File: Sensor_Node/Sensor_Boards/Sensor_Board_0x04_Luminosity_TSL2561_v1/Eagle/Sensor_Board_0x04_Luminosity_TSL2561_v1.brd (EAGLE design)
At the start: 55 x 35 mm, 15 parts, among them J1 M04_SMD_90, J2 M06_SMD_STRAIGHT, J4 ARDUINO_ISP, U2 ATMEGA328P_TQFP, Y1 8MHZ

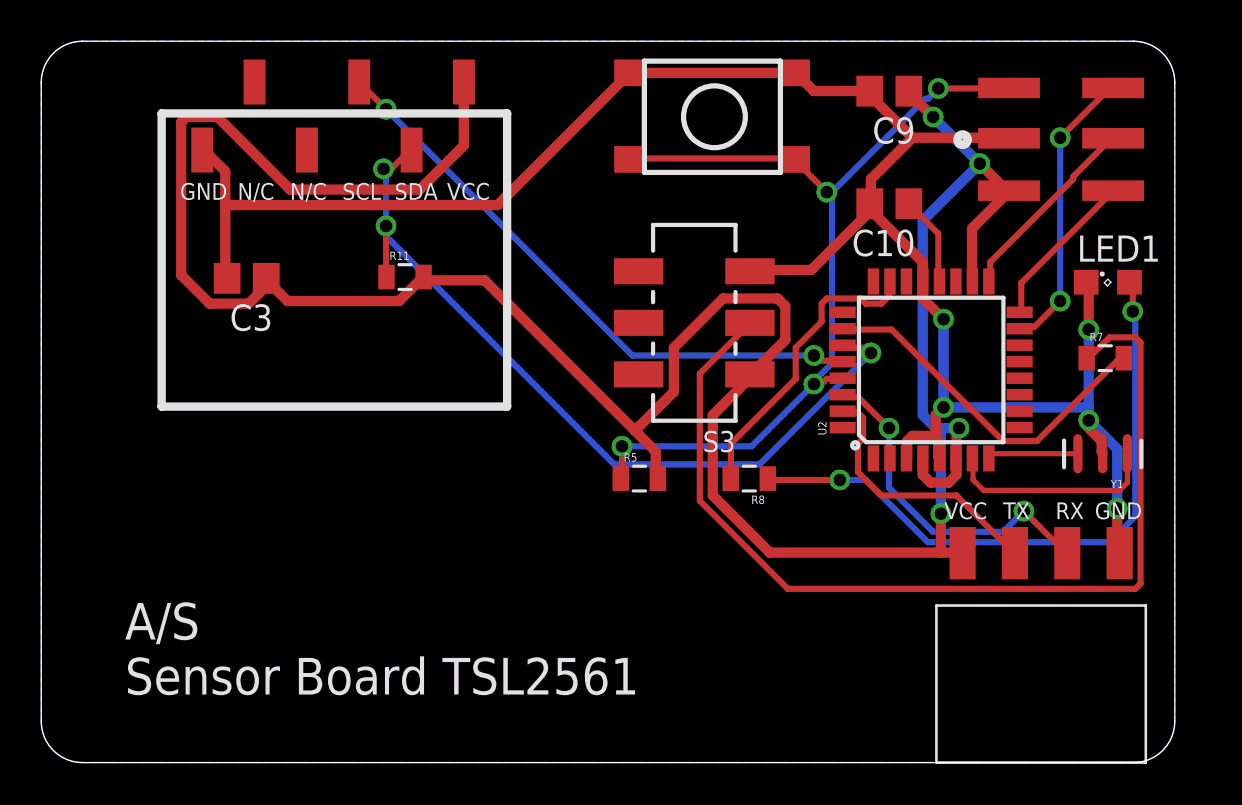
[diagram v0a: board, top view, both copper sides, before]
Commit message: Changes on SensModule TSL2561
- removed R11
- added pogohead programming connector
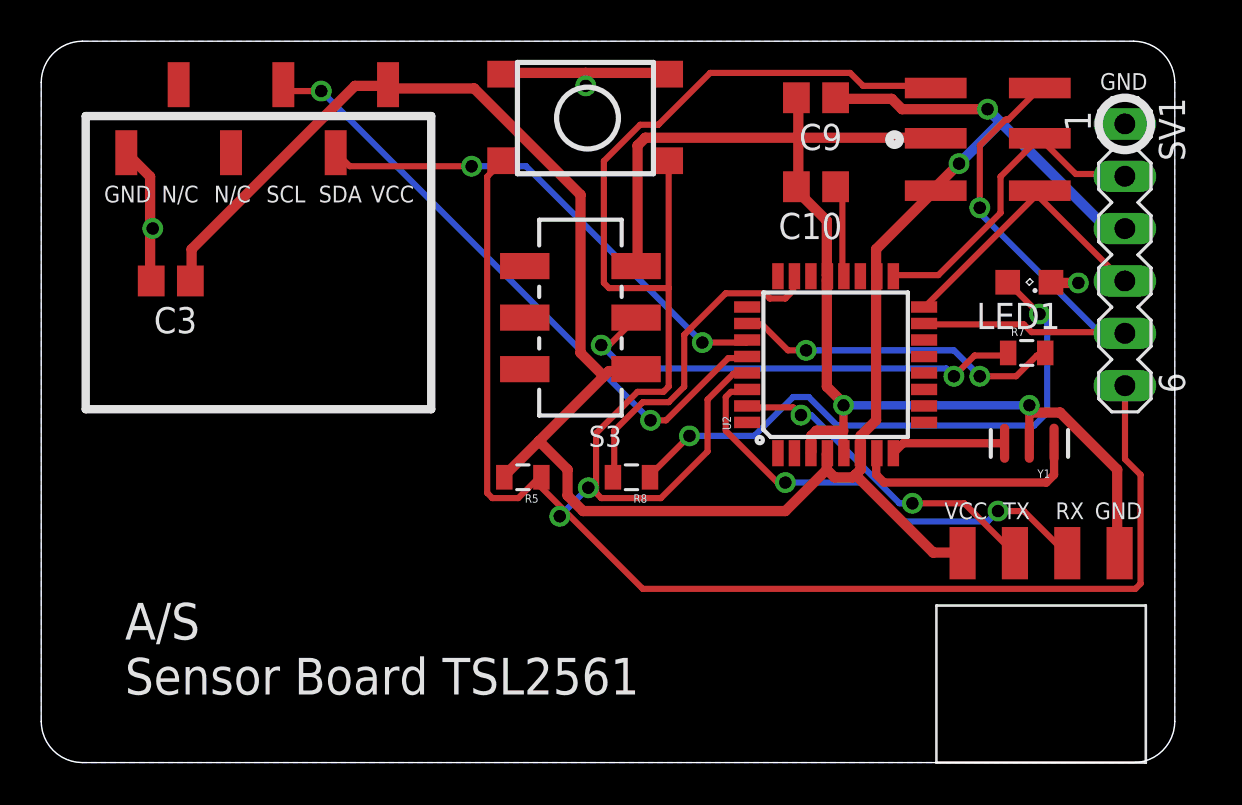
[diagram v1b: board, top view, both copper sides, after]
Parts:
- removed R11: 10k, SparkFun-Passives:0805
- added SV1: (no value), con-lstb:MA06-1
- moved S1 6.16 mm to (22.4, 33.4)
- moved R8 5.72 mm to (28.6, 13.8)
- moved R5 5.65 mm to (23.4, 13.8), turned to 180 degrees
- moved S3 5.53 mm to (26.2, 21.6)
- moved U2 4.64 mm to (38.5, 19.3)
- moved R7 3.82 mm to (47.8, 19.9)
- moved LED1 3.81 mm to (47.9, 23.3), turned to 180 degrees
- moved C3 3.69 mm to (6.29, 23.4)
- moved J2 3.69 mm to (4.13, 29.6)
- moved C10 3.65 mm to (37.6, 27.9)
- moved Y1 3.59 mm to (47.9, 15.5)
- moved C9 3.57 mm to (37.6, 32.3)
- moved J4 3.56 mm to (48.5, 27.7)
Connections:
- net GND: now also SV1.1
- net MISO: now also SV1.4
- net MOSI: now also SV1.5
- net RESET: now also SV1.6
- net SCK: now also SV1.2
- net SDA: no longer R11.1
- net VCC: now also SV1.3; no longer R11.2
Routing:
- net RESET: track 44.5 -> 121.2 mm, vias 4 -> 2
- net N$3: track 47.7 -> 23.1 mm, vias 0 -> 2
- net VCC: track 130.6 -> 106.7 mm, vias 4 -> 2
- net GND: track 99.5 -> 78.8 mm
- net SDA: track 39.4 -> 23.9 mm, vias 3 -> 2
- net MOSI: track 14.1 -> 26.7 mm, vias 2 -> 1
- net MISO: track 7.79 -> 14.2 mm
- net SCK: track 9.51 -> 15.8 mm
- net MCU_RXI: track 16.6 -> 22.3 mm
- net MCU_TXO: track 13.1 -> 15.9 mm, vias 0 -> 2
- net N$30: track 31.1 -> 28.9 mm
- net DBG_ENABLE: track 17.6 -> 16.0 mm, vias 0 -> 2
- net L1: track 14.7 -> 16.2 mm
- net SCL: track 29.1 -> 30.5 mm
- net N$2: track 10.3 -> 11.5 mm
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
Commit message: Changes on all boards
- added capacitor on reset-path
- changed order of pogopin programmer pins

Pulse-Board:
- Deleted input-jumper. Currently one interrupt-pin missing, so print is
not yet routed.
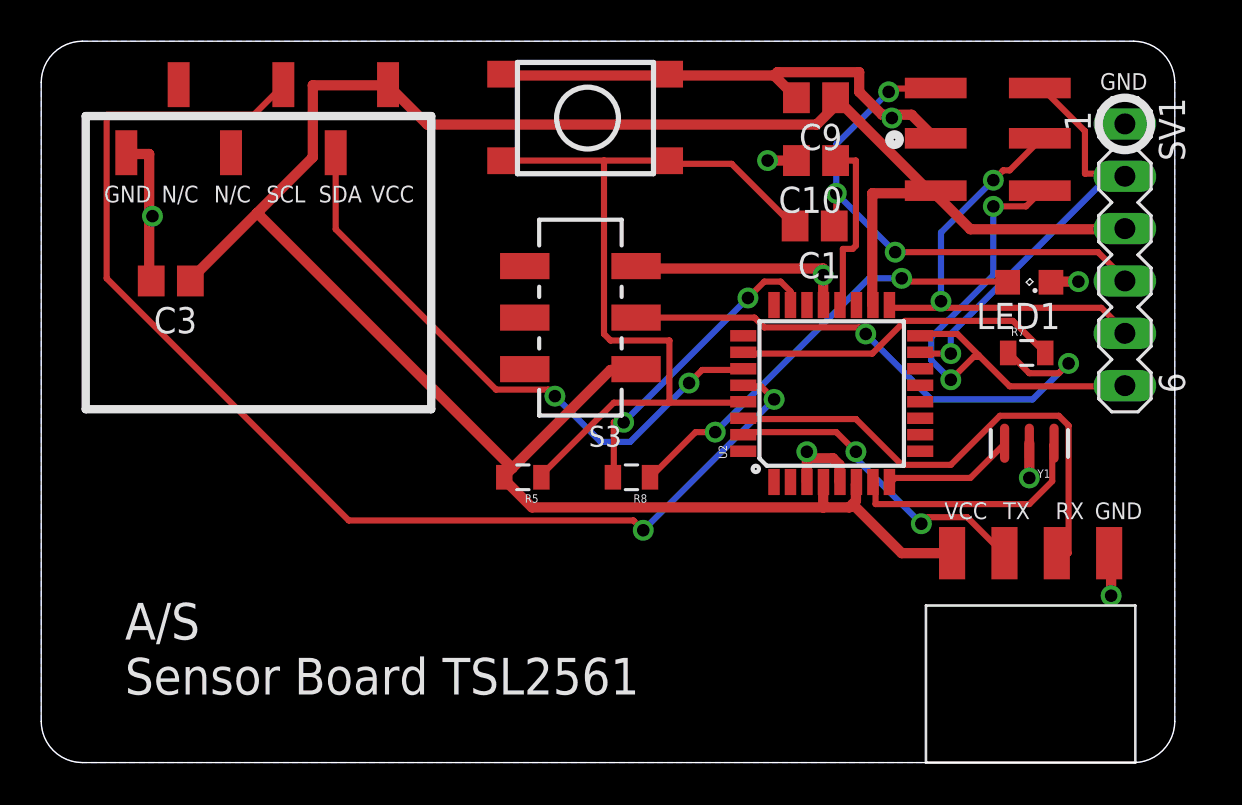
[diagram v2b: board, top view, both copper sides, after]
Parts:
- added C1: 100n, eagle-ltspice:C0805
- moved U2 1.41 mm to (38.4, 17.9)
- moved C10 1.27 mm to (37.6, 29.2)
- moved J1 0.51 mm to (44.2, 10.2)
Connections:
- new net N$4: C1.2, R5.1, S1.3, S1.4, U2.29
- net MISO: now also SV1.6; no longer SV1.4
- net MOSI: now also SV1.2; no longer SV1.5
- net RESET: now also C1.1, SV1.4; no longer R5.1, S1.3, S1.4, SV1.6, U2.29
- net SCK: now also SV1.5; no longer SV1.2
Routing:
- net RESET: track 121.2 -> 25.8 mm, vias 2 -> 3
- net N$4: track 0.00 -> 41.6 mm
- net SCL: track 30.5 -> 59.0 mm
- net GND: track 78.8 -> 53.7 mm, vias 5 -> 8
- net MISO: track 14.2 -> 25.6 mm, vias 0 -> 2
- net VCC: track 106.7 -> 116.2 mm, vias 2 -> 0
- net N$30: track 28.9 -> 21.4 mm
- net SCK: track 15.8 -> 22.4 mm, vias 0 -> 2
- net MOSI: track 26.7 -> 21.2 mm
- net SDA: track 23.9 -> 29.2 mm
- net N$15: track 4.55 -> 8.66 mm
- net N$3: track 23.1 -> 26.9 mm
- net MCU_RXI: track 22.3 -> 24.7 mm, vias 2 -> 0
- net L1: track 16.2 -> 14.9 mm, vias 0 -> 2
- net N$1: track 5.60 -> 6.37 mm
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
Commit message: Changed some SensorBoards
SHT31
- new routing

PULSE
- pogopin programmer now over FTDI
- interrupt to comboard now comes from atmega

TSL2561
- pogopin programmer now over FTDI

PROTOYPING
- changed title of schematic
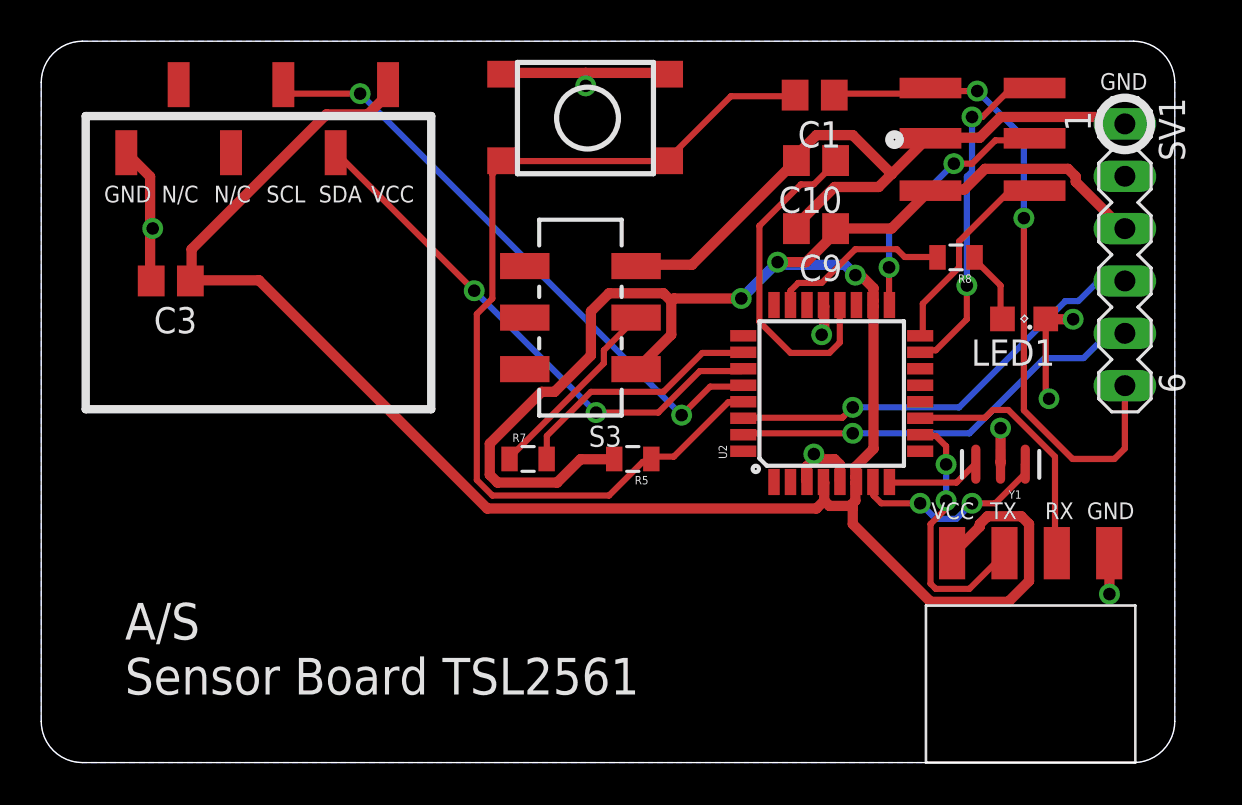
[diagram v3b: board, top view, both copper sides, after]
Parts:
- moved R7 24.7 mm to (23.6, 14.7)
- moved R8 19.0 mm to (44.4, 24.5)
- moved C9 6.35 mm to (37.6, 25.9)
- moved C1 6.35 mm to (37.5, 32.4)
- moved R5 5.41 mm to (28.7, 14.7)
- moved LED1 1.80 mm to (47.7, 21.5)
- moved Y1 1.73 mm to (46.5, 14.5)
- moved J4 0.25 mm to (48.2, 27.7)
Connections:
- new net FTDI_RXI: SV1.4, U2.30
- new net FTDI_TXO: SV1.5, U2.31
- net GND: now also SV1.2
- net MCU_RXI: now also U2.11; no longer U2.30
- net MCU_TXO: now also U2.10; no longer U2.31
- net MISO: no longer SV1.6
- net MOSI: no longer SV1.2
- net RESET: now also SV1.6; no longer SV1.4
- net SCK: no longer SV1.5
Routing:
- net SCL: track 59.0 -> 29.5 mm
- net VCC: track 116.2 -> 139.2 mm, vias 0 -> 3
- net FTDI_RXI: track 0.00 -> 21.3 mm, vias 0 -> 1
- net FTDI_TXO: track 0.00 -> 20.6 mm, vias 0 -> 1
- net N$30: track 21.4 -> 3.54 mm, vias 2 -> 0
- net N$3: track 26.9 -> 9.39 mm, vias 2 -> 0
- net MISO: track 25.6 -> 10.1 mm, vias 2 -> 0
- net MCU_RXI: track 24.7 -> 12.4 mm
- net GND: track 53.7 -> 64.1 mm
- net SCK: track 22.4 -> 12.6 mm
- net N$15: track 8.66 -> 16.4 mm
- net RESET: track 25.8 -> 32.8 mm, vias 3 -> 2
- net L1: track 14.9 -> 8.82 mm, vias 2 -> 0
- net N$4: track 41.6 -> 46.7 mm
- net MOSI: track 21.2 -> 16.5 mm, vias 1 -> 2
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
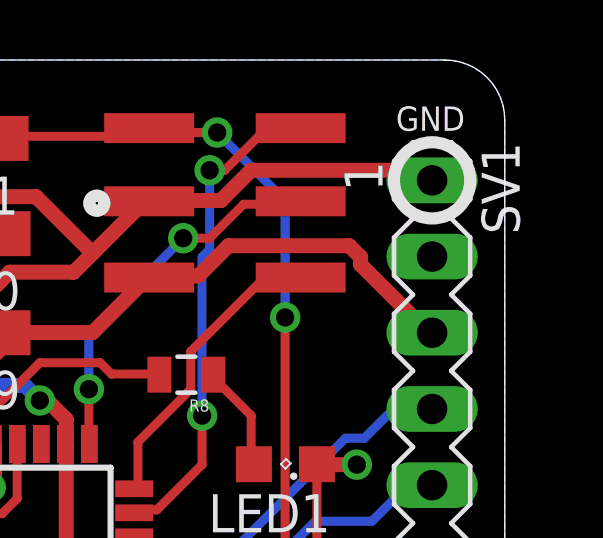
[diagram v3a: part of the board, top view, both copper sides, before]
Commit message: Finished some boards.
- Minor changes on all boards except
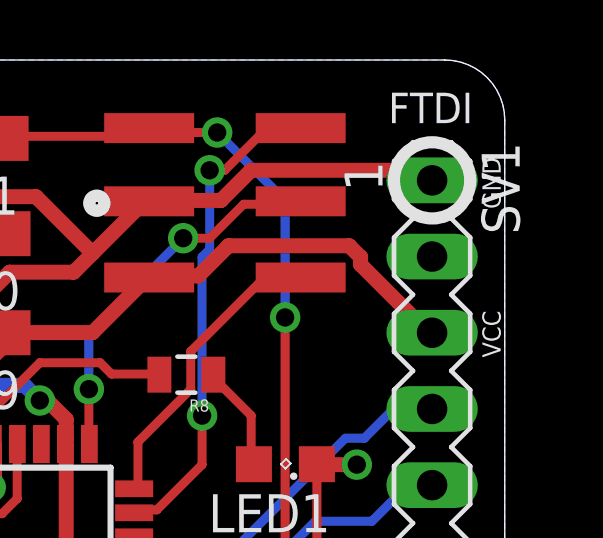
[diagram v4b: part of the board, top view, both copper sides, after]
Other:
- board text added: "FTDI"
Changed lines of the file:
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@@
 <text x="4.064" y="3.302" size="1.778" layer="21">A/S
 Sensor Board TSL2561</text>
-<text x="51.3715" y="32.639" size="0.8128" layer="21">GND</text>
+<text x="51.1175" y="32.893" size="1.016" layer="21">FTDI</text>
 <circle x="52.578" y="30.988" radius="1.27" width="0.4064" layer="21"/>
+<text x="54.864" y="30.0355" size="0.6096" layer="21" rot="R90">GND</text>
+<text x="54.864" y="25.0825" size="0.6096" layer="21" rot="R90">VCC</text>
 </plain>
 <attributes>

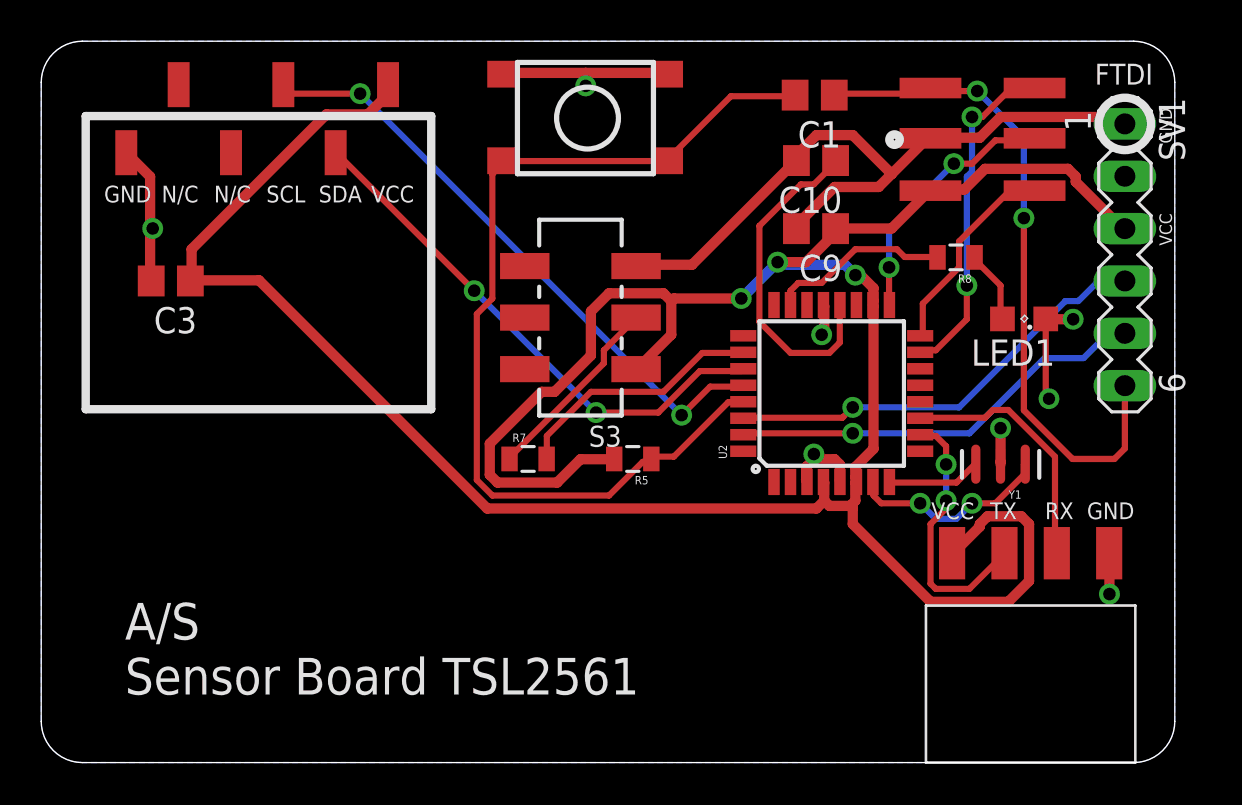
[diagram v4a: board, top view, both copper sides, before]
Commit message: Changes Library & TSL2561
- moved reset path a bit around
- corrected faulty connector in library and on print
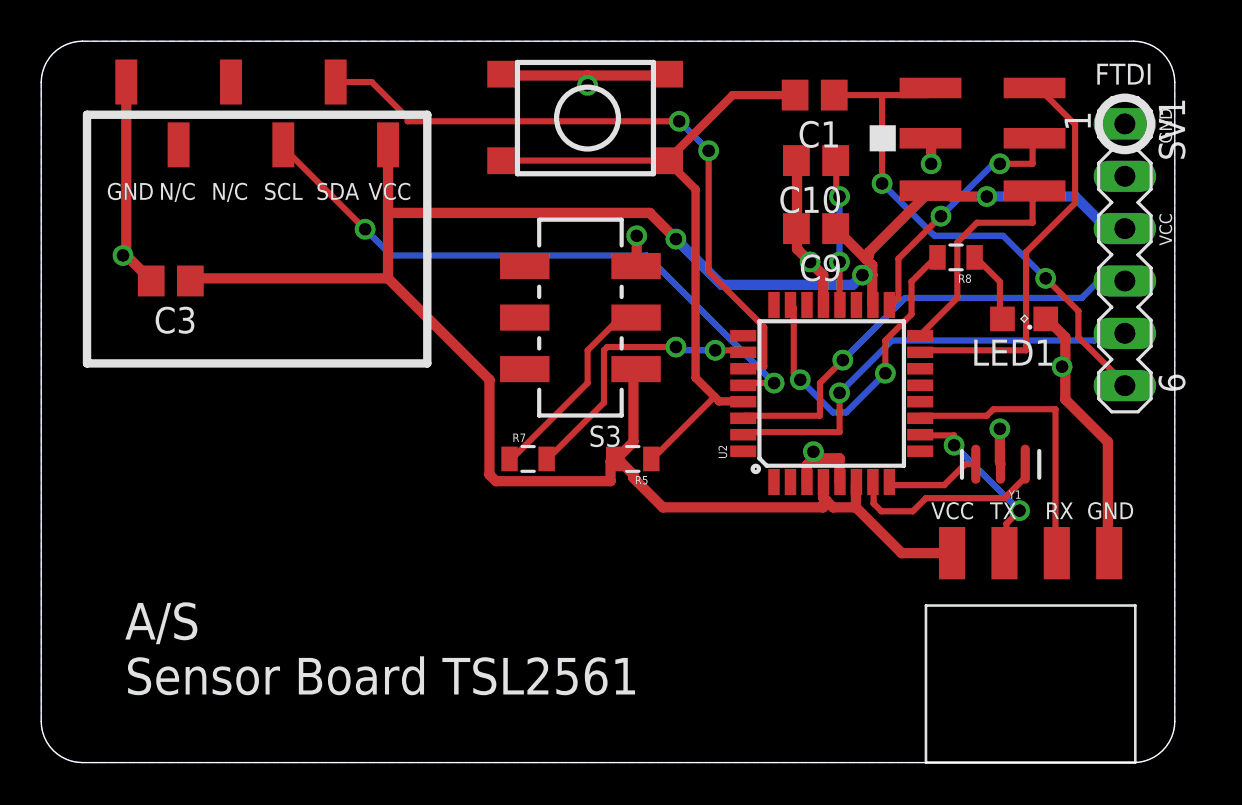
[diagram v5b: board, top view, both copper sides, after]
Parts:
- removed J2: M06_SMD_STRAIGHT, myownthings:M06_SMD_STRAIGHT
- added U$9: M06_SMD_STRAIGHT, wsn:M06_SMD_STRAIGHT
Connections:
- net GND: now also U$9.P1; no longer J2.P1
- net SCL: now also U$9.P4; no longer J2.P4
- net SDA: now also U$9.P5; no longer J2.P5
- net VCC: now also U$9.P6; no longer J2.P6
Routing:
- net VCC: track 139.2 -> 105.1 mm
- net GND: track 64.1 -> 47.7 mm
- net N$4: track 46.7 -> 33.7 mm
- net N$15: track 16.4 -> 7.12 mm, vias 0 -> 2
- net L1: track 8.82 -> 16.1 mm, vias 0 -> 2
- net RESET: track 32.8 -> 25.9 mm
- net SDA: track 25.9 -> 32.2 mm
- net MCU_TXO: track 12.9 -> 9.04 mm
- net MOSI: track 16.5 -> 20.0 mm, vias 2 -> 0
- net MCU_RXI: track 12.4 -> 13.8 mm
- net FTDI_TXO: track 20.6 -> 21.7 mm
- net DBG_ENABLE: track 12.3 -> 13.4 mm, vias 0 -> 2
- net FTDI_RXI: track 21.3 -> 22.2 mm
- net MISO: track 10.1 -> 10.9 mm
- net SCL: track 29.5 -> 30.2 mm
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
